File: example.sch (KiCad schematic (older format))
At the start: 10 parts, among them P1 CONN_01X03, P3 CONN_01X06, P4 CONN_01X01, P5 CONN_01X20, P6 CONN_01X12, P7 CONN_01X16, P8 CONN_01X09, P9 CONN_01X04

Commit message: Some rename/cleanup before pushing to github.
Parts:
- removed P5: CONN_01X20, Socket_Strips:Socket_Strip_Straight_1x20, symbol CONN_01X20
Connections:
- no-connect marks 46 -> 26
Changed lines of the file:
@@
 NoConn ~ 4850 2350
-$Comp
-L CONN_01X20 P5
-U 1 1 58759D71
-P 6250 2200
-F 0 "P5" H 6250 3250 50  0000 C CNN
-F 1 "CONN_01X20" V 6350 2200 50  0000 C CNN
-F 2 "Socket_Strips:Socket_Strip_Straight_1x20" H 6250 2200 50  0001 C CNN
-F 3 "" H 6250 2200 50  0000 C CNN
-	1    6250 2200
-	1    0    0    -1
-$EndComp
-NoConn ~ 6050 1250
-NoConn ~ 6050 1350
-NoConn ~ 6050 1450
-NoConn ~ 6050 1550
-NoConn ~ 6050 1850
-NoConn ~ 6050 1750
-NoConn ~ 6050 1650
-NoConn ~ 6050 3150
-NoConn ~ 6050 3050
-NoConn ~ 6050 2950
-NoConn ~ 6050 2850
-NoConn ~ 6050 2750
-NoConn ~ 6050 2650
-NoConn ~ 6050 2550
-NoConn ~ 6050 2450
-NoConn ~ 6050 2350
-NoConn ~ 6050 2250
-NoConn ~ 6050 2150
-NoConn ~ 6050 2050
-NoConn ~ 6050 1950
 $Comp
 L CONN_01X12 P6

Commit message: Adjust for wifi board for April demo.
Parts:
- removed P9: CONN_01X04, Socket_Strips:Socket_Strip_Straight_1x04, symbol CONN_01X04
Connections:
- net labels added: LOAD
- net labels removed: RB_RX, RB_TX, USB
- wire segments 34 -> 29
- no-connect marks 26 -> 28
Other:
- moved on the sheet: R1, R2
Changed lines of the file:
@@
 L R R1
 U 1 1 587596E9
-P 3450 2650
-F 0 "R1" V 3530 2650 50  0000 C CNN
-F 1 "R" V 3450 2650 50  0000 C CNN
-F 2 "Resistors_THT:Resistor_Horizontal_RM7mm" V 3380 2650 50  0001 C CNN
-F 3 "" H 3450 2650 50  0000 C CNN
-	1    3450 2650
+P 3450 2550
+F 0 "R1" V 3530 2550 50  0000 C CNN
+F 1 "R" V 3450 2550 50  0000 C CNN
+F 2 "Resistors_THT:Resistor_Horizontal_RM7mm" V 3380 2550 50  0001 C CNN
+F 3 "" H 3450 2550 50  0000 C CNN
+	1    3450 2550
 	0    1    1    0
 $EndComp
@@
 L R R2
 U 1 1 58759766
-P 4250 2650
-F 0 "R2" V 4330 2650 50  0000 C CNN
-F 1 "R" V 4250 2650 50  0000 C CNN
-F 2 "Resistors_THT:Resistor_Horizontal_RM7mm" V 4180 2650 50  0001 C CNN
-F 3 "" H 4250 2650 50  0000 C CNN
-	1    4250 2650
+P 4250 2550
+F 0 "R2" V 4330 2550 50  0000 C CNN
+F 1 "R" V 4250 2550 50  0000 C CNN
+F 2 "Resistors_THT:Resistor_Horizontal_RM7mm" V 4180 2550 50  0001 C CNN
+F 3 "" H 4250 2550 50  0000 C CNN
+	1    4250 2550
 	0    1    1    0
 $EndComp
@@
 L GND #PWR01
 U 1 1 58759956
-P 3150 2750
-F 0 "#PWR01" H 3150 2500 50  0001 C CNN
-F 1 "GND" H 3150 2600 50  0000 C CNN
-F 2 "" H 3150 2750 50  0000 C CNN
-F 3 "" H 3150 2750 50  0000 C CNN
-	1    3150 2750
+P 3150 2950
+F 0 "#PWR01" H 3150 2700 50  0001 C CNN
+F 1 "GND" H 3150 2800 50  0000 C CNN
+F 2 "" H 3150 2950 50  0000 C CNN
+F 3 "" H 3150 2950 50  0000 C CNN
+	1    3150 2950
 	1    0    0    -1
 $EndComp
@@
 	1    0    0    -1
 $EndComp
-Text Label 3950 2850 0    60   ~ 0
+Text Label 3950 2750 0    60   ~ 0
 BAT
 Wire Wire Line
-	3600 2650 4100 2650
-Wire Wire Line
-	3150 2250 3150 2750
-Wire Wire Line
-	3150 2650 3300 2650
-Wire Wire Line
-	4400 2650 4850 2650
-Wire Wire Line
-	3150 2550 4850 2550
-Connection ~ 3150 2650
+	3600 2550 4100 2550
 Wire Wire Line
 	4850 2250 3150 2250
 Connection ~ 3150 2550
-Connection ~ 4550 2650
-Wire Wire Line
-	3850 2650 3850 2850
-Connection ~ 3850 2650
+Wire Wire Line
+	3850 2550 3850 2750
+Connection ~ 3850 2550
 Wire Wire Line
 	5500 4600 5500 4500
 Wire Wire Line
 	5500 4500 5700 4500
-Connection ~ 3850 2850
+Connection ~ 3850 2750
 Wire Wire Line
 	4850 2150 4300 2150
 Text Label 4300 2150 0    60   ~ 0
-USB
+LOAD
 Wire Wire Line
 	3700 3900 3700 3600
@@
 	3700 3600 4000 3600
 Text Label 3800 3600 0    60   ~ 0
-USB
+LOAD
 $Comp
 L GND #PWR03
@@
 Text Label 5200 3900 0    60   ~ 0
 3V3
-Wire Wire Line
-	5700 4300 5200 4300
-Wire Wire Line
-	5700 4400 5200 4400
-Text Label 5200 4300 0    60   ~ 0
-GPS_TX
-Text Label 5200 4400 0    60   ~ 0
-GPS_RX
 NoConn ~ 4300 4850
 NoConn ~ 4100 4850
@@
 NoConn ~ 3000 3900
 Wire Wire Line
-	3400 3900 3400 3500
-Wire Wire Line
-	3300 3900 3300 3500
-Text Label 3400 3750 1    60   ~ 0
-RB_RX
-Text Label 3300 3750 1    60   ~ 0
-RB_TX
-Wire Wire Line
 	3000 4850 3000 5350
 Wire Wire Line
@@
 NoConn ~ 3900 3900
 Wire Wire Line
-	1900 4050 2350 4050
-Wire Wire Line
-	1900 4150 2350 4150
-Text Label 2350 4150 2    60   ~ 0
-RB_TX
-Text Label 2350 4050 2    60   ~ 0
-RB_RX
-Wire Wire Line
 	3500 4850 3500 5650
 Wire Wire Line
 	3500 5650 5100 5650
-$Comp
-L CONN_01X04 P9
-U 1 1 58765D82
-P 1700 4100
-F 0 "P9" H 1700 4350 50  0000 C CNN
-F 1 "CONN_01X04" V 1800 4100 50  0000 C CNN
-F 2 "Socket_Strips:Socket_Strip_Straight_1x04" H 1700 4100 50  0001 C CNN
-F 3 "" H 1700 4100 50  0000 C CNN
-	1    1700 4100
-	-1   0    0    1
-$EndComp
-$Comp
-L GND #PWR04
-U 1 1 58765E2F
-P 2100 4250
-F 0 "#PWR04" H 2100 4000 50  0001 C CNN
-F 1 "GND" H 2100 4100 50  0000 C CNN
-F 2 "" H 2100 4250 50  0000 C CNN
-F 3 "" H 2100 4250 50  0000 C CNN
-	1    2100 4250
-	1    0    0    -1
-$EndComp
-Wire Wire Line
-	2100 4250 1900 4250
-Wire Wire Line
-	1900 3950 2350 3950
-Text Label 2150 3950 0    60   ~ 0
-USB
-Wire Wire Line
-	3850 2850 4100 2850
+Wire Wire Line
+	3850 2750 4100 2750
 Wire Wire Line
 	5100 6150 4750 6150
@@
 Wire Wire Line
 	5100 6350 5100 6250
+Wire Wire Line
+	5700 4300 5200 4300
+Wire Wire Line
+	5700 4400 5200 4400
+Text Label 5200 4400 0    60   ~ 0
+GPS_RX
+Text Label 5200 4300 0    60   ~ 0
+GPS_TX
+NoConn ~ 3400 3900
+NoConn ~ 3300 3900
+Wire Wire Line
+	4850 2550 4400 2550
+Wire Wire Line
+	3300 2550 3150 2550
+Wire Wire Line
+	3150 2250 3150 2950
+Wire Wire Line
+	4850 2650 4850 2850
+Wire Wire Line
+	4850 2850 3150 2850
+Connection ~ 3150 2850
 $EndSCHEMATC

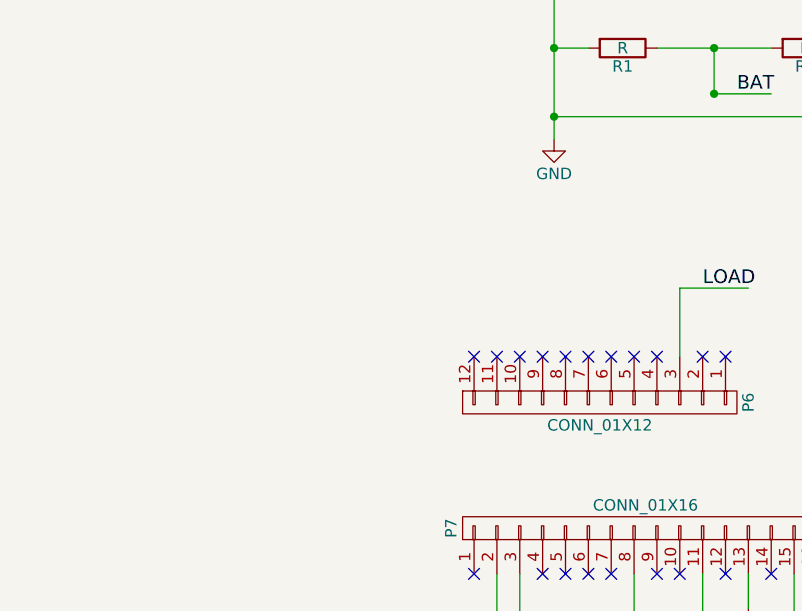
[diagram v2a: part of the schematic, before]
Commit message: Add some LEDs for status indicators.
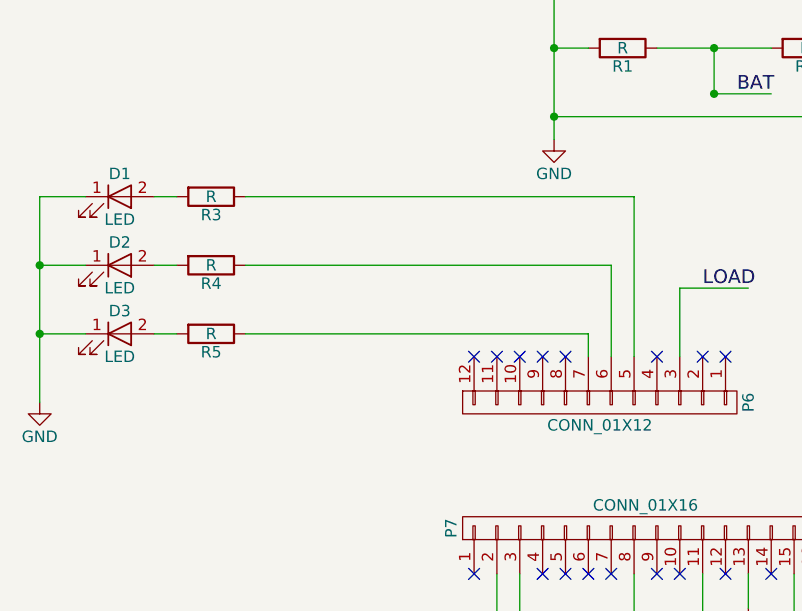
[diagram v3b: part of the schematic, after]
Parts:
- added D1, D2, D3: LED, Diodes_ThroughHole:D_T-1_P2.54mm_Vertical_AnodeUp, symbol LED
- added R3, R4, R5: R, Resistors_ThroughHole:R_Axial_DIN0207_L6.3mm_D2.5mm_P7.62mm_Horizontal, symbol R
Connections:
- wire segments 29 -> 42
- no-connect marks 28 -> 25
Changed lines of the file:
@@
 Text Label 3950 2750 0    60   ~ 0
 BAT
-Wire Wire Line
-	3600 2550 4100 2550
-Wire Wire Line
-	4850 2250 3150 2250
-Connection ~ 3150 2550
-Wire Wire Line
-	3850 2550 3850 2750
-Connection ~ 3850 2550
-Wire Wire Line
-	5500 4600 5500 4500
-Wire Wire Line
-	5500 4500 5700 4500
-Connection ~ 3850 2750
-Wire Wire Line
-	4850 2150 4300 2150
 Text Label 4300 2150 0    60   ~ 0
 LOAD
-Wire Wire Line
-	3700 3900 3700 3600
-Wire Wire Line
-	3700 3600 4000 3600
 Text Label 3800 3600 0    60   ~ 0
 LOAD
@@
 	1    0    0    -1
 $EndComp
-Wire Wire Line
-	4000 5000 4000 4850
-Wire Wire Line
-	4200 4850 4200 5050
-Wire Wire Line
-	4200 5050 4650 5050
 Text Label 4500 5050 0    60   ~ 0
 3V3
-Wire Wire Line
-	5700 3900 5200 3900
 Text Label 5200 3900 0    60   ~ 0
 3V3
@@
 NoConn ~ 2800 3900
 NoConn ~ 2900 3900
-Wire Wire Line
-	3800 4850 3800 5350
-Wire Wire Line
-	3800 5350 4650 5350
 Text Label 4500 5350 0    60   ~ 0
 BAT
@@
 NoConn ~ 3100 4850
 NoConn ~ 3600 3900
-NoConn ~ 3500 3900
 NoConn ~ 3200 3900
 NoConn ~ 3100 3900
 NoConn ~ 3000 3900
-Wire Wire Line
-	3000 4850 3000 5350
-Wire Wire Line
-	2900 4850 2900 5350
 Text Label 3000 5350 1    60   ~ 0
 GPS_TX
@@
 NoConn ~ 3800 3900
 NoConn ~ 3900 3900
-Wire Wire Line
-	3500 4850 3500 5650
-Wire Wire Line
-	3500 5650 5100 5650
-Wire Wire Line
-	3850 2750 4100 2750
-Wire Wire Line
-	5100 6150 4750 6150
-Wire Wire Line
-	5100 6250 4750 6250
 Text Label 4750 6150 0    60   ~ 0
 3V3
 $Comp
-L GND #PWR05
+L GND #PWR04
 U 1 1 58768B90
 P 4750 6250
-F 0 "#PWR05" H 4750 6000 50  0001 C CNN
+F 0 "#PWR04" H 4750 6000 50  0001 C CNN
 F 1 "GND" H 4750 6100 50  0000 C CNN
 F 2 "" H 4750 6250 50  0000 C CNN
@@
 	1    0    0    -1
 $EndComp
-Wire Wire Line
-	5100 6350 5100 6250
-Wire Wire Line
-	5700 4300 5200 4300
-Wire Wire Line
-	5700 4400 5200 4400
 Text Label 5200 4400 0    60   ~ 0
 GPS_RX
 Text Label 5200 4300 0    60   ~ 0
 GPS_TX
-NoConn ~ 3400 3900
-NoConn ~ 3300 3900
+$Comp
+L LED D3
+U 1 1 58DAC70E
+P 1250 3800
+F 0 "D3" H 1250 3900 50  0000 C CNN
+F 1 "LED" H 1250 3700 50  0000 C CNN
+F 2 "Diodes_ThroughHole:D_T-1_P2.54mm_Vertical_AnodeUp" H 1250 3800 50  0001 C CNN
+F 3 "" H 1250 3800 50  0000 C CNN
+	1    1250 3800
+	1    0    0    -1
+$EndComp
+$Comp
+L LED D2
+U 1 1 58DAC8A3
+P 1250 3500
+F 0 "D2" H 1250 3600 50  0000 C CNN
+F 1 "LED" H 1250 3400 50  0000 C CNN
+F 2 "Diodes_ThroughHole:D_T-1_P2.54mm_Vertical_AnodeUp" H 1250 3500 50  0001 C CNN
+F 3 "" H 1250 3500 50  0000 C CNN
+	1    1250 3500
+	1    0    0    -1
+$EndComp
+$Comp
+L LED D1
+U 1 1 58DAC94B
+P 1250 3200
+F 0 "D1" H 1250 3300 50  0000 C CNN
+F 1 "LED" H 1250 3100 50  0000 C CNN
+F 2 "Diodes_ThroughHole:D_T-1_P2.54mm_Vertical_AnodeUp" H 1250 3200 50  0001 C CNN
+F 3 "" H 1250 3200 50  0000 C CNN
+	1    1250 3200
+	1    0    0    -1
+$EndComp
+$Comp
+L R R5
+U 1 1 58DAC9A7
+P 1650 3800
+F 0 "R5" V 1730 3800 50  0000 C CNN
+F 1 "R" V 1650 3800 50  0000 C CNN
+F 2 "Resistors_ThroughHole:R_Axial_DIN0207_L6.3mm_D2.5mm_P7.62mm_Horizontal" V 1580 3800 50  0001 C CNN
+F 3 "" H 1650 3800 50  0000 C CNN
+	1    1650 3800
+	0    1    1    0
+$EndComp
+$Comp
+L R R4
+U 1 1 58DAC9FC
+P 1650 3500
+F 0 "R4" V 1730 3500 50  0000 C CNN
+F 1 "R" V 1650 3500 50  0000 C CNN
+F 2 "Resistors_ThroughHole:R_Axial_DIN0207_L6.3mm_D2.5mm_P7.62mm_Horizontal" V 1580 3500 50  0001 C CNN
+F 3 "" H 1650 3500 50  0000 C CNN
+	1    1650 3500
+	0    1    1    0
+$EndComp
+$Comp
+L R R3
+U 1 1 58DACA3B
+P 1650 3200
+F 0 "R3" V 1730 3200 50  0000 C CNN
+F 1 "R" V 1650 3200 50  0000 C CNN
+F 2 "Resistors_ThroughHole:R_Axial_DIN0207_L6.3mm_D2.5mm_P7.62mm_Horizontal" V 1580 3200 50  0001 C CNN
+F 3 "" H 1650 3200 50  0000 C CNN
+	1    1650 3200
+	0    1    1    0
+$EndComp
+$Comp
+L GND #PWR05
+U 1 1 58DACA7B
+P 900 4100
+F 0 "#PWR05" H 900 3850 50  0001 C CNN
+F 1 "GND" H 900 3950 50  0000 C CNN
+F 2 "" H 900 4100 50  0000 C CNN
+F 3 "" H 900 4100 50  0000 C CNN
+	1    900  4100
+	1    0    0    -1
+$EndComp
+Wire Wire Line
+	3600 2550 4100 2550
+Wire Wire Line
+	4850 2250 3150 2250
+Connection ~ 3150 2550
+Wire Wire Line
+	3850 2550 3850 2750
+Connection ~ 3850 2550
+Wire Wire Line
+	5500 4600 5500 4500
+Wire Wire Line
+	5500 4500 5700 4500
+Connection ~ 3850 2750
+Wire Wire Line
+	4850 2150 4300 2150
+Wire Wire Line
+	3700 3900 3700 3600
+Wire Wire Line
+	3700 3600 4000 3600
+Wire Wire Line
+	4000 5000 4000 4850
+Wire Wire Line
+	4200 4850 4200 5050
+Wire Wire Line
+	4200 5050 4650 5050
+Wire Wire Line
+	5700 3900 5200 3900
+Wire Wire Line
+	3800 4850 3800 5350
+Wire Wire Line
+	3800 5350 4650 5350
+Wire Wire Line
+	3000 4850 3000 5350
+Wire Wire Line
+	2900 4850 2900 5350
+Wire Wire Line
+	3500 4850 3500 5650
+Wire Wire Line
+	3500 5650 5100 5650
+Wire Wire Line
+	3850 2750 4100 2750
+Wire Wire Line
+	5100 6150 4750 6150
+Wire Wire Line
+	5100 6250 4750 6250
+Wire Wire Line
+	5100 6350 5100 6250
+Wire Wire Line
+	5700 4300 5200 4300
+Wire Wire Line
+	5700 4400 5200 4400
 Wire Wire Line
 	4850 2550 4400 2550
@@
 	4850 2850 3150 2850
 Connection ~ 3150 2850
+Wire Wire Line
+	900  3200 900  4100
+Wire Wire Line
+	900  3800 1100 3800
+Wire Wire Line
+	900  3500 1100 3500
+Connection ~ 900  3800
+Wire Wire Line
+	900  3200 1100 3200
+Connection ~ 900  3500
+Wire Wire Line
+	1400 3200 1500 3200
+Wire Wire Line
+	1500 3500 1400 3500
+Wire Wire Line
+	1400 3800 1500 3800
+Wire Wire Line
+	3300 3900 3300 3800
+Wire Wire Line
+	3300 3800 1800 3800
+Wire Wire Line
+	1800 3500 3400 3500
+Wire Wire Line
+	3400 3500 3400 3900
+Wire Wire Line
+	3500 3900 3500 3200
+Wire Wire Line
+	3500 3200 1800 3200
 $EndSCHEMATC
